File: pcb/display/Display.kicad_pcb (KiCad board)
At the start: 2 copper layers, 100 x 75 mm, 181 parts, among them J1 Screw_Terminal_01x04, J10 XH 2P, J11 XH 2P, J12 XH 2P, J13 XH 2P, J14 XH 2P, J15 XH 2P, J16 XH 2P, J17 XH 2P, J18 XH 2P, J19 XH 2P, J2 RJ45, J20 XH 2P, J4 Conn_01x08_Pin, J5 Term, J6 Term, J7 XH 2P, J8 XH 2P, J9 XH 2P, P1 USB_C_Plug_USB2.0, Q1 60N03D, Q10 60N03D, Q11 60N03D, Q12 60N03D, Q13 60N03D, Q14 60N03D, Q15 60N03D, Q16 60N03D, Q2 60N03D, Q3 60N03D, Q4 60N03D, Q5 60N03D, Q6 60N03D, Q7 60N03D, Q8 60N03D, Q9 60N03D, SW1 SW_Push, SW2 SW_Push, SW3 SW_Push, SW4 SW_Push, U1 TMP1075DSG, U10 TPS259474x, U11 LV3842, U2 ESP32-S3-MINI-1, U3 TPS22810DRV, U4 TCA9535RGER, U5 SP3485EN, U6 AP2210, U7 Ai-Thinker-Ra-02, U8 E220-400M22S, U9 SIC438BED-T1-GE3

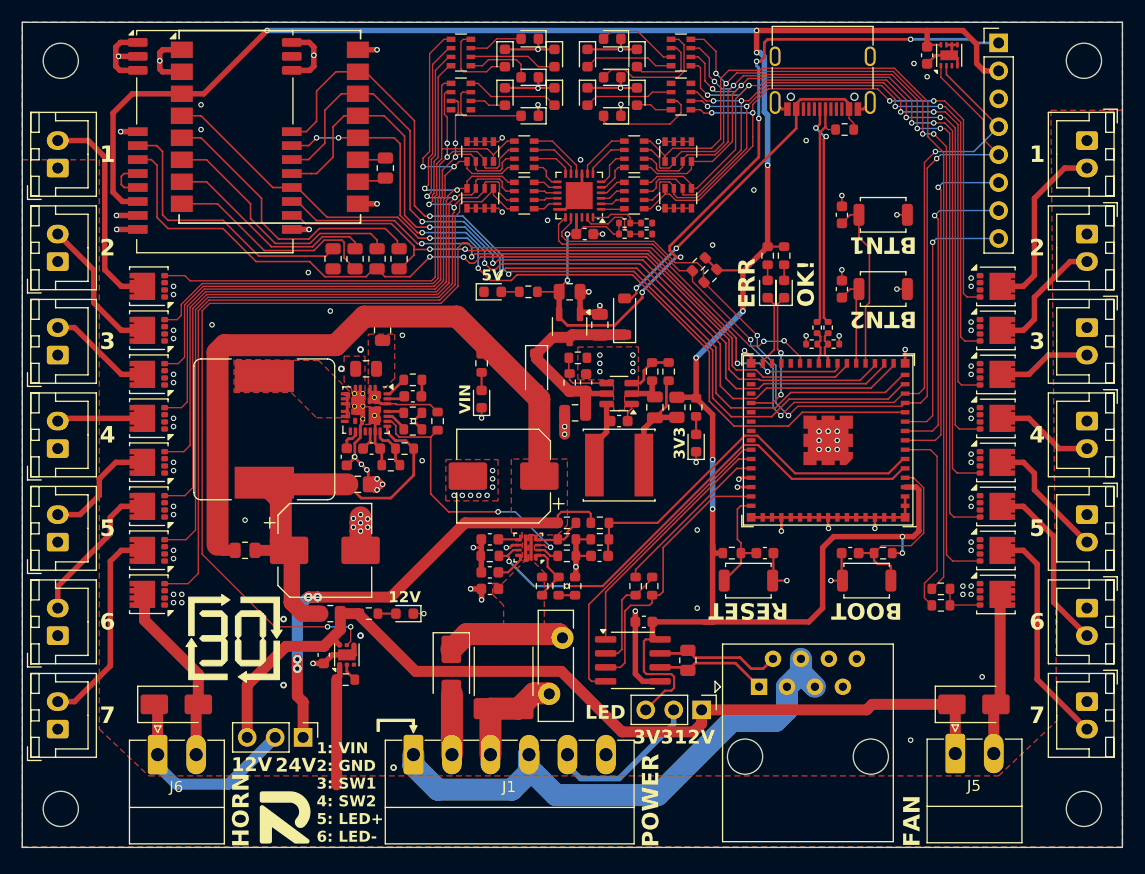
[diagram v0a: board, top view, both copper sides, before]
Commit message: Final Version of Prototype Rev. 00
Switched back to PCA9685 for PWM, removed high side switch
Updated some component values
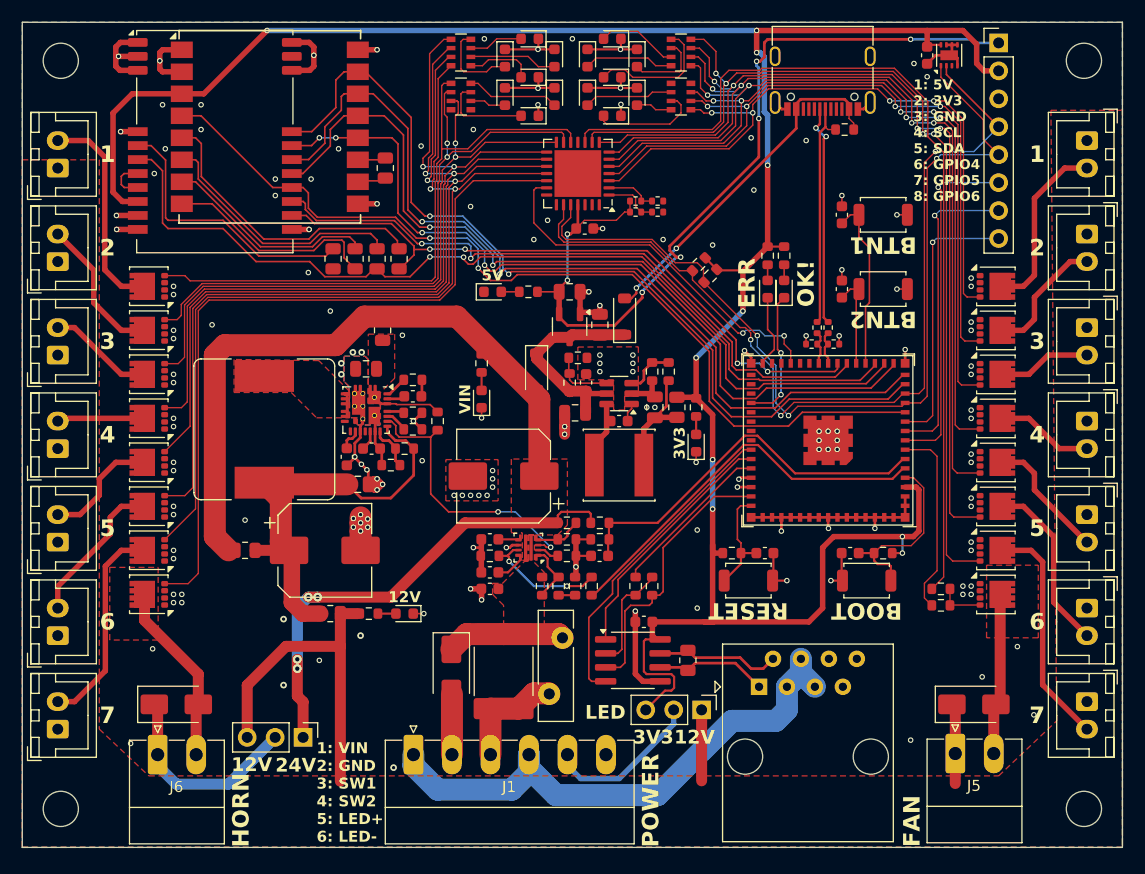
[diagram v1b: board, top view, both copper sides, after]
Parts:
- removed C5: 100nF, Capacitor_SMD:C_0603_1608Metric
- removed the G*** at (77.5, 122.0)
- removed the REF** at (69.0, 106.0)
- removed RN1, RN2, RN3, RN4: 10R, Resistor_SMD:R_Array_Convex_4x0603
- removed RN5, RN6, RN7, RN8: 10k, Resistor_SMD:R_Array_Convex_4x0603
- removed U3: TPS22810DRV, Package_SON:WSON-6-1EP_2x2mm_P0.65mm_EP1x1.6mm
- added G***: LOGO, RVNSPRK_Markings:JLC-UL_1-2Layer_10mm, B.Cu at (100.0, 91.2)
- added G***: LOGO, Open-Shot-Clock:Open-Shot-Clock_QR_8mm, B.Cu at (108.7, 120.8)
- added REF**: OSHW-Logo2_7.3x6mm_SilkScreen, Symbol:OSHW-Logo2_7.3x6mm_SilkScreen, B.Cu at (136.5, 121.5)
- C10, C11: value 100n -> 10p
- C6: value 100nF -> 100n
- D1, D2: value D_Schottky -> SMAJ24A
- D18, D19: value D_Schottky -> B5819W
- G***: footprint RVNSPRK_Logo:Ravnsprk_Logo_5mm -> RVNSPRK_Logo:Ravnsprk_Logo_Mask_5mm; moved to B.Cu
- J1: value Screw_Terminal_01x04 -> Screw Terminal 3.5mm
- J4: value Conn_01x08_Pin -> 01x08_Pin
- J5, J6: value Term -> Term 3.5mm
- L3: value 10u -> 10uH
- Q1, Q10, Q11, Q12, Q13, Q14, Q15, Q16, Q2, Q3, Q4, Q5, Q6, Q7, Q8, Q9: value 60N03D -> 20N06
- R10, R46, R47: value 20k -> 4k3
- R17, R35, R43: value 20k -> 1k
- R18, R34: value 20k -> 10k
- R2: value 10R -> 1k
- R33: value 20k -> 22k
- R48, R49, R50, R51: value 10R -> 0R
- R8, R9: value 1k -> 0R
- RN09, RN10, RN11, RN12: value 10R -> 3k3
- SW1, SW2, SW3, SW4: value SW_Push -> SW_4x3mm
- U4: value TCA9535RGER -> PCA9685BS; footprint Package_DFN_QFN:VQFN-24-1EP_4x4mm_P0.5mm_EP2.45x2.45mm -> Package_DFN_QFN:QFN-28-1EP_6x6mm_P0.65mm_EP4.25x4.25mm
- moved R2 23.9 mm to (101.8, 101.2), turned to -90 degrees
- moved REF** 21.3 mm to (121.2, 121.2)
- moved REF** 6.15 mm to (100.5, 61.6)
- moved G*** 3.34 mm to (77.2, 121.5), turned to 180 degrees
- moved R48 2.24 mm to (107.8, 66.2)
- moved R49 2.24 mm to (107.8, 67.2)
- moved R50 2.24 mm to (105.8, 67.2)
- moved R51 2.24 mm to (105.8, 66.2)
- moved U4 2.00 mm to (100.5, 63.8)
- moved C6 0.50 mm to (101.1, 68.8)
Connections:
- J10 pad 1: +12P -> +12V
- J11 pad 1: +12P -> +12V
- J12 pad 1: +12P -> +12V
- J13 pad 1: +12P -> +12V
- J14 pad 1: +12P -> +12V
- J15 pad 1: +12P -> +12V
- J16 pad 1: +12P -> +12V
- J17 pad 1: +12P -> +12V
- J18 pad 1: +12P -> +12V
- J19 pad 1: +12P -> +12V
- J20 pad 1: +12P -> +12V
- J7 pad 1: +12P -> +12V
- J8 pad 1: +12P -> +12V
- J9 pad 1: +12P -> +12V
- R2 pad 1: +12P -> Net-(U10-ILIM)
- R2 pad 2: Net-(U3-QOD) -> /I_SENSE
- R25 pad 1: /I_SENSE -> Net-(U10-ILIM)
- R45 pad 2: Net-(RN2-R4.1) -> Net-(U4-LED7)
- R48 pad 1: Net-(U4-A2) -> Net-(U4-A4)
- R49 pad 1: Net-(U4-A1) -> Net-(U4-A3)
- R50 pad 2: Net-(U4-A1) -> Net-(U4-A3)
- R51 pad 2: Net-(U4-A2) -> Net-(U4-A4)
- U10 pad 9: /I_SENSE -> Net-(U10-ILIM)
- U2 pad 26: /BRIGHTNESS -> unconnected-(U2-GPIO26-Pad26)
- U2 pad 27: unconnected-(U2-GPIO47/SPICLK_P/SUBSPICLK_P_DIFF-Pad27) -> /PWM.OE
- U4 pad 1: Net-(RN1-R1.2) -> Net-(U4-A3)
- U4 pad 10: Net-(RN3-R1.2) -> Net-(U4-LED7)
- U4 pad 11: Net-(RN3-R2.2) -> GND
- U4 pad 12: Net-(RN3-R3.2) -> /LED Driver/7-Segment1/Segment1
- U4 pad 13: Net-(RN3-R4.2) -> /LED Driver/7-Segment1/Segment2
- U4 pad 14: Net-(RN4-R1.2) -> /LED Driver/7-Segment1/Segment3
- U4 pad 15: Net-(RN4-R2.2) -> /LED Driver/7-Segment1/Segment4
- U4 pad 16: Net-(RN4-R3.2) -> /LED Driver/7-Segment1/Segment5
- U4 pad 17: Net-(RN4-R4.2) -> /LED Driver/7-Segment1/Segment6
- U4 pad 18: GND -> /LED Driver/7-Segment1/Segment7
- U4 pad 19: /I2C.SCL -> Net-(Q2-G)
- U4 pad 2: Net-(RN1-R2.2) -> Net-(U4-A4)
- U4 pad 20: /I2C.SDA -> /PWM.OE
- U4 pad 21: +5V -> GND
- U4 pad 23: Net-(U4-A1) -> /I2C.SCL
- U4 pad 24: Net-(U4-A2) -> /I2C.SDA
- U4 pad 25: GND -> +5V
- U4 pad 3: Net-(RN1-R3.2) -> /LED Driver/7-Segment2/Segment1
- U4 pad 4: Net-(RN1-R4.2) -> /LED Driver/7-Segment2/Segment2
- U4 pad 5: Net-(RN2-R1.2) -> /LED Driver/7-Segment2/Segment3
- U4 pad 6: Net-(RN2-R2.2) -> /LED Driver/7-Segment2/Segment4
- U4 pad 7: Net-(RN2-R3.2) -> /LED Driver/7-Segment2/Segment5
- U4 pad 8: Net-(RN2-R4.2) -> /LED Driver/7-Segment2/Segment6
- U4 pad 9: GND -> /LED Driver/7-Segment2/Segment7
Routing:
- net /BRIGHTNESS: track 104.4 -> 0.00 mm, vias 4 -> 0
- net Net-(U4-LED7): track 0.00 -> 83.3 mm
- net Net-(RN2-R4.1): track 80.1 -> 0.00 mm
- net +12V: track 85.4 -> 45.3 mm
- net /PWM.OE: track 0.00 -> 34.2 mm, vias 0 -> 2
- net GND: track 186.5 -> 163.2 mm, vias 146 -> 164
- net Net-(U10-ILIM): track 0.00 -> 11.3 mm, vias 0 -> 2
- net +12P: track 11.1 -> 0.00 mm
- net /I_SENSE: track 46.5 -> 35.8 mm, vias 2 -> 0
- net Net-(U4-A1): track 6.59 -> 0.00 mm
- net Net-(RN3-R1.2): track 5.52 -> 0.00 mm
- net /LED Driver/7-Segment1/Segment1: track 51.5 -> 56.9 mm
- net Net-(U4-A2): track 5.10 -> 0.00 mm
- net Net-(RN2-R4.2): track 5.02 -> 0.00 mm
- net Net-(U4-A3): track 0.00 -> 5.00 mm
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- added copper zone on F.Cu, net +12V
- added copper zone on F.Cu, net Net-(D1-A2)
- added copper zone on F.Cu, net Net-(D2-A2)
- removed copper zone on F.Cu, net +12P
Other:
- board text added: "1: 5V 2: 3V3 3: GND 4: SCL 5: SDA 6: GPIO4 7: GPIO5 8: GPIO6"
- board text added: "Open Shot Clock Display"
- board text added: "Rev. 00 яαvεηsραяκ 2024"
- board text removed: "Open Shot Clock Display Driver"
- board text removed: "R00 яαvεηsραяκ 2024"

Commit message: Display HW Revision 01
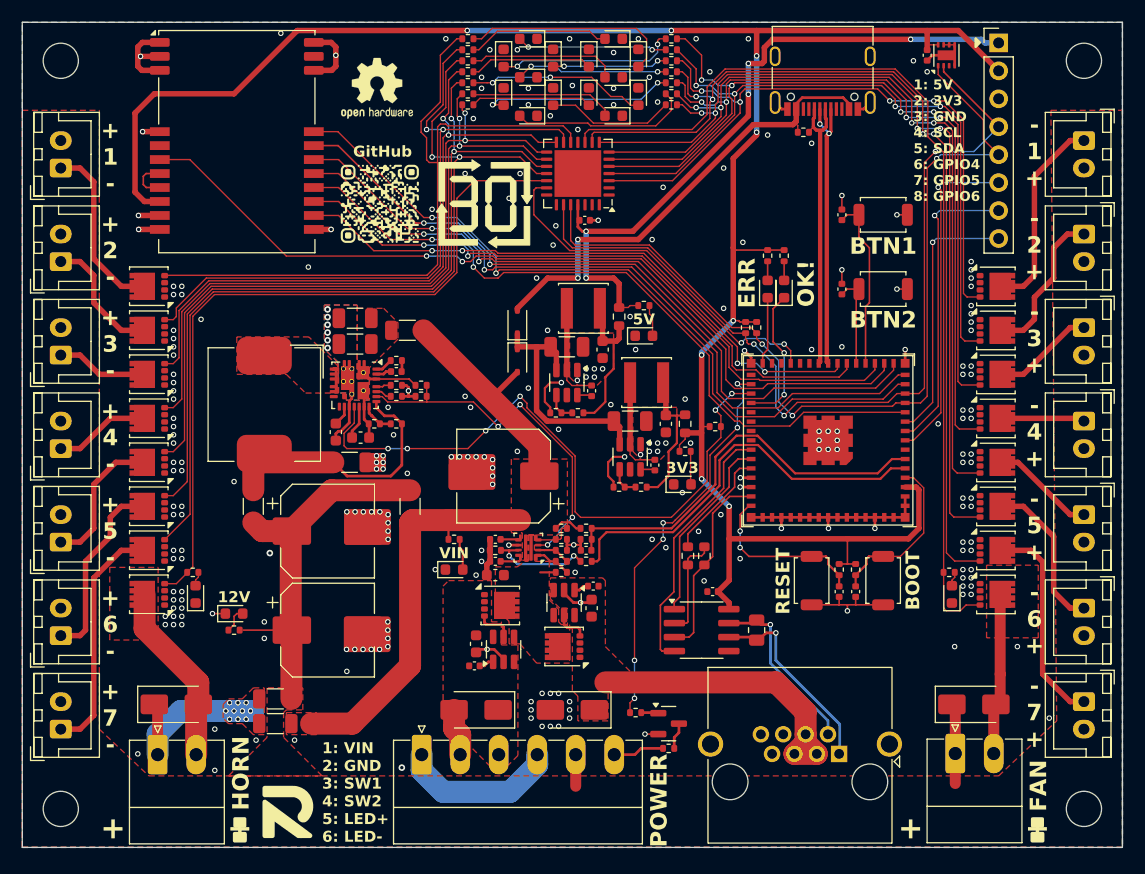
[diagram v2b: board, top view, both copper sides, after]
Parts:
- removed C10, C11: 10p, Resistor_SMD:R_0402_1005Metric
- removed C21, C9: 100n, Capacitor_SMD:C_0603_1608Metric
- removed C22, C24: 1u, Capacitor_SMD:C_0805_2012Metric
- removed C23, C25: 10u, Capacitor_SMD:C_0805_2012Metric
- removed D17: SMAJ24A, Diode_SMD:D_SMA
- removed D22: LED, LED_SMD:LED_0603_1608Metric
- removed F1: 2.6A, Fuse:Fuse_2920_7451Metric
- removed F2: 3A, Fuse:Fuse_Bourns_MF-RG400
- removed JP1, JP2: Jumper_3_Open, Connector_PinHeader_2.54mm:PinHeader_1x03_P2.54mm_Vertical
- removed L4: 12uH, Inductor_SMD:L_Changjiang_FNR6045S
- removed R11, R12, R13, R14, R16, R3: 0R, Resistor_SMD:R_0805_2012Metric
- removed R24, R44, R45: 0R, Resistor_SMD:R_0603_1608Metric
- removed R31, R41: 22k, Resistor_SMD:R_0603_1608Metric
- removed R32, R42: 10k, Resistor_SMD:R_0603_1608Metric
- removed R35: 1k, Resistor_SMD:R_0603_1608Metric
- removed R48, R49, R50, R51, R8, R9: 0R, Resistor_SMD:R_0402_1005Metric
- removed RN09, RN10, RN11, RN12: 3k3, Resistor_SMD:R_Array_Convex_4x0603
- removed U11: LV3842, Package_TO_SOT_SMD:SOT-23-6
- removed U6: AP2210, Package_TO_SOT_SMD:SOT-23-3
- removed U7: Ai-Thinker-Ra-02, RF_Module:Ai-Thinker-Ra-01-LoRa
- added C602: 10u, Capacitor_SMD:C_1206_3216Metric, F.Cu at (80.2, 76.9)
- added C608: 100u, Capacitor_SMD:CP_Elec_8x10, F.Cu at (77.8, 105.2)
- added C614: 100n, Capacitor_SMD:C_0402_1005Metric, F.Cu at (107.5, 90.2)
- added C615: 10u, Capacitor_SMD:C_1206_3216Metric, F.Cu at (105.2, 86.2)
- added C616: 10u, Capacitor_SMD:C_0603_1608Metric, F.Cu at (108.5, 86.5)
- added C617: 100n, Capacitor_SMD:C_0402_1005Metric, F.Cu at (101.8, 83.5)
- added C618: 10u, Capacitor_SMD:C_1206_3216Metric, F.Cu at (99.5, 79.5)
- added C619: 10u, Capacitor_SMD:C_0603_1608Metric, F.Cu at (102.8, 79.8)
- added C620: 100n, Capacitor_SMD:C_0402_1005Metric, F.Cu at (91.1, 108.5)
- added C621: 100n, Capacitor_SMD:C_0402_1005Metric, F.Cu at (101.9, 101.2)
- added C622: 1u, Capacitor_SMD:C_0603_1608Metric, F.Cu at (91.2, 106.5)
- added C623: 1u, Capacitor_SMD:C_0603_1608Metric, F.Cu at (101.8, 103.2)
- added D201: LED, LED_SMD:LED_0603_1608Metric, F.Cu at (65.8, 102.0)
- added D203: LED, LED_SMD:LED_0603_1608Metric, F.Cu at (134.5, 102.0)
- added D603: SMAJ24CA, Diode_SMD:D_SMA, F.Cu at (91.2, 112.5)
- added D604: SMAJ24CA, Diode_SMD:D_SMA, F.Cu at (100.0, 112.5)
- added D608: LED, LED_SMD:LED_0603_1608Metric, F.Cu at (110.0, 92.0)
- added G***: LOGO, RVNSPRK_Logo:Ravnsprk_Logo_5mm, F.Cu at (74.2, 121.8)
- added L602: 33uH, Inductor_SMD:L_Changjiang_FNR4030S, F.Cu at (106.8, 82.8)
- added L603: 33uH, Inductor_SMD:L_Changjiang_FNR4030S, F.Cu at (101.0, 76.0)
- added Q101: 2N7002, Package_TO_SOT_SMD:SOT-23, F.Cu at (108.8, 113.8)
- added Q601: DOZ35N06, Package_SON:VSON-8_3.3x3.3mm_P0.65mm_NexFET, F.Cu at (93.5, 103.0)
- added Q602: DOZ35N06, Package_SON:VSON-8_3.3x3.3mm_P0.65mm_NexFET, F.Cu at (99.2, 106.8)
- added R104: 1k8, Resistor_SMD:R_0402_1005Metric, F.Cu at (105.8, 112.8)
- added R105: 1k8, Resistor_SMD:R_0402_1005Metric, F.Cu at (108.8, 116.0)
- added R110: 18k, Resistor_SMD:R_0402_1005Metric, F.Cu at (113.0, 86.8)
- added R201: 0R, Resistor_SMD:R_1206_3216Metric, F.Cu at (73.0, 113.8)
- added R202: 0R, Resistor_SMD:R_1206_3216Metric, F.Cu at (73.0, 111.5)
- added R203: 4k3, Resistor_SMD:R_0402_1005Metric, F.Cu at (65.5, 100.0)
- added R204: 4k3, Resistor_SMD:R_0402_1005Metric, F.Cu at (134.2, 100.0)
- added R401: 4k3, Resistor_SMD:R_0402_1005Metric, F.Cu at (90.5, 53.5)
- added R402: 4k3, Resistor_SMD:R_0402_1005Metric, F.Cu at (90.5, 55.5)
- added R403: 4k3, Resistor_SMD:R_0402_1005Metric, F.Cu at (90.5, 56.5)
- added R404: 4k3, Resistor_SMD:R_0402_1005Metric, F.Cu at (90.5, 57.5)
- added R405: 4k3, Resistor_SMD:R_0402_1005Metric, F.Cu at (90.5, 54.5)
- added R406: 4k3, Resistor_SMD:R_0402_1005Metric, F.Cu at (90.5, 52.5)
- added R407: 4k3, Resistor_SMD:R_0402_1005Metric, F.Cu at (90.5, 51.5)
- added R501: 4k3, Resistor_SMD:R_0402_1005Metric, F.Cu at (109.0, 54.5)
- added R502: 4k3, Resistor_SMD:R_0402_1005Metric, F.Cu at (109.0, 57.5)
- added R503: 4k3, Resistor_SMD:R_0402_1005Metric, F.Cu at (109.0, 56.5)
- added R504: 4k3, Resistor_SMD:R_0402_1005Metric, F.Cu at (109.0, 55.5)
- added R505: 4k3, Resistor_SMD:R_0402_1005Metric, F.Cu at (109.0, 51.5)
- added R506: 4k3, Resistor_SMD:R_0402_1005Metric, F.Cu at (109.0, 52.5)
- added R507: 4k3, Resistor_SMD:R_0402_1005Metric, F.Cu at (109.0, 53.5)
- added R612: 4k3, Resistor_SMD:R_0402_1005Metric, F.Cu at (86.2, 84.0)
- added R620: 0R, Resistor_SMD:R_0603_1608Metric, F.Cu at (110.2, 86.5)
- added R621: 82k, Resistor_SMD:R_0402_1005Metric, F.Cu at (106.2, 92.2)
- added R622: 18k, Resistor_SMD:R_0402_1005Metric, F.Cu at (104.2, 92.2)
- added R623: 0R, Resistor_SMD:R_0603_1608Metric, F.Cu at (104.2, 76.8)
- added R624: 82k, Resistor_SMD:R_0402_1005Metric, F.Cu at (100.5, 85.5)
- added R625: 11k, Resistor_SMD:R_0402_1005Metric, F.Cu at (98.5, 85.5)
- added R629: 1k8, Resistor_SMD:R_0402_1005Metric, F.Cu at (110.2, 89.0)
- added U603: TPS54202DDC, Package_TO_SOT_SMD:SOT-23-6, F.Cu at (105.2, 89.5)
- added U604: TPS54202DDC, Package_TO_SOT_SMD:SOT-23-6, F.Cu at (99.5, 82.8)
- added U605: LM74700, Package_TO_SOT_SMD:SOT-23-6, F.Cu at (93.8, 107.0)
- added U606: LM74700, Package_TO_SOT_SMD:SOT-23-6, F.Cu at (99.2, 102.8)
- C101: renamed from C3; footprint Capacitor_SMD:C_0603_1608Metric -> Capacitor_SMD:C_0402_1005Metric
- C102: renamed from C4; footprint Capacitor_SMD:C_0603_1608Metric -> Capacitor_SMD:C_0402_1005Metric
- C103: renamed from C2; footprint Capacitor_SMD:C_0603_1608Metric -> Capacitor_SMD:C_0402_1005Metric
- C104: renamed from C1; footprint Capacitor_SMD:C_0603_1608Metric -> Capacitor_SMD:C_0402_1005Metric
- C105: renamed from C27; footprint Capacitor_SMD:C_0603_1608Metric -> Capacitor_SMD:C_0402_1005Metric
- C201: renamed from C6; footprint Capacitor_SMD:C_0603_1608Metric -> Capacitor_SMD:C_0402_1005Metric
- C301: renamed from C7; footprint Capacitor_SMD:C_0603_1608Metric -> Capacitor_SMD:C_0402_1005Metric
- C601: renamed from C12; footprint Capacitor_SMD:C_0603_1608Metric -> Capacitor_SMD:C_0402_1005Metric
- C603: renamed from C16; value 1u -> 10u; footprint Capacitor_SMD:C_0805_2012Metric -> Capacitor_SMD:C_1206_3216Metric
- C606: renamed from C19; value 1u -> 10u; footprint Capacitor_SMD:C_0805_2012Metric -> Capacitor_SMD:C_1206_3216Metric
- C609: renamed from C26; value 100n -> 1u
- C610: renamed from C13; value 1u -> 10n; footprint Capacitor_SMD:C_0603_1608Metric -> Capacitor_SMD:C_0402_1005Metric
- C611: renamed from C14; footprint Capacitor_SMD:C_0603_1608Metric -> Capacitor_SMD:C_0402_1005Metric
- C613: renamed from C8; footprint Capacitor_SMD:C_0603_1608Metric -> Capacitor_SMD:C_0402_1005Metric
- D202: renamed from D2; value SMAJ24A -> SS54
- D204: renamed from D1; value SMAJ24A -> SS54
- D601: renamed from D19; value B5819W -> 1N5819WS; footprint Diode_SMD:D_SOD-123 -> Diode_SMD:D_SOD-323
- D602: renamed from D18; value B5819W -> 1N5819WS; footprint Diode_SMD:D_SOD-123 -> Diode_SMD:D_SOD-323
- G***, REF** (x2): moved to F.Cu
- J101: renamed from J2; footprint Connector_RJ:RJ45_Amphenol_54602-x08_Horizontal -> Connector_RJ:RJ45_Amphenol_RJHSE5380
- L601: renamed from L3; value 10uH -> 6.8uH; footprint Inductor_SMD:L_Bourns_SRR1260 -> Inductor_SMD:L_Bourns_SRP1050WA
- Q201: renamed from Q2; value 20N06 -> DOZ35N06
- Q202: renamed from Q1; value 20N06 -> DOZ35N06
- Q401: renamed from Q3; value 20N06 -> DOZ35N06
- Q402: renamed from Q4; value 20N06 -> DOZ35N06
- Q403: renamed from Q5; value 20N06 -> DOZ35N06
- Q404: renamed from Q6; value 20N06 -> DOZ35N06
- Q405: renamed from Q7; value 20N06 -> DOZ35N06
- Q406: renamed from Q8; value 20N06 -> DOZ35N06
- Q407: renamed from Q9; value 20N06 -> DOZ35N06
- Q501: renamed from Q10; value 20N06 -> DOZ35N06
- Q502: renamed from Q11; value 20N06 -> DOZ35N06
- Q503: renamed from Q12; value 20N06 -> DOZ35N06
- Q504: renamed from Q13; value 20N06 -> DOZ35N06
- Q505: renamed from Q14; value 20N06 -> DOZ35N06
- Q506: renamed from Q15; value 20N06 -> DOZ35N06
- Q507: renamed from Q16; value 20N06 -> DOZ35N06
- R101: renamed from R17; value 1k -> 1k8; footprint Resistor_SMD:R_0603_1608Metric -> Resistor_SMD:R_0402_1005Metric
- R102: renamed from R43; value 1k -> 1k8; footprint Resistor_SMD:R_0603_1608Metric -> Resistor_SMD:R_0402_1005Metric
- R103: renamed from R7; footprint Resistor_SMD:R_0603_1608Metric -> Resistor_SMD:R_0402_1005Metric
- R106: renamed from R1; value 1k -> 1k8; footprint Resistor_SMD:R_0603_1608Metric -> Resistor_SMD:R_0402_1005Metric
- R107: renamed from R46; footprint Resistor_SMD:R_0603_1608Metric -> Resistor_SMD:R_0402_1005Metric
- R108: renamed from R47; footprint Resistor_SMD:R_0603_1608Metric -> Resistor_SMD:R_0402_1005Metric
- R109: renamed from R15; value 1k -> 1k8; footprint Resistor_SMD:R_0603_1608Metric -> Resistor_SMD:R_0402_1005Metric
- R601: renamed from R37; footprint Resistor_SMD:R_0805_2012Metric -> Resistor_SMD:R_1206_3216Metric
- R602: renamed from R36; footprint Resistor_SMD:R_0805_2012Metric -> Resistor_SMD:R_1206_3216Metric
- R603: renamed from R18; value 10k -> 18k; footprint Resistor_SMD:R_0603_1608Metric -> Resistor_SMD:R_0402_1005Metric
- R604: renamed from R19; value 10k -> 18k; footprint Resistor_SMD:R_0603_1608Metric -> Resistor_SMD:R_0402_1005Metric
- R605: renamed from R38; footprint Resistor_SMD:R_0603_1608Metric -> Resistor_SMD:R_0402_1005Metric
- R606: renamed from R20; value 10k -> 18k; footprint Resistor_SMD:R_0603_1608Metric -> Resistor_SMD:R_0402_1005Metric
- R607: renamed from R21; value 10k -> 18k; footprint Resistor_SMD:R_0603_1608Metric -> Resistor_SMD:R_0402_1005Metric
- R608: renamed from R40; footprint Resistor_SMD:R_0805_2012Metric -> Resistor_SMD:R_1206_3216Metric
- R609: renamed from R22; value 1k -> 1k8; footprint Resistor_SMD:R_0603_1608Metric -> Resistor_SMD:R_0402_1005Metric
- R610: renamed from R2; value 1k -> 1k8; footprint Resistor_SMD:R_0603_1608Metric -> Resistor_SMD:R_0402_1005Metric
- R611: renamed from R23; footprint Resistor_SMD:R_0603_1608Metric -> Resistor_SMD:R_0402_1005Metric
- R613: renamed from R28; footprint Resistor_SMD:R_0603_1608Metric -> Resistor_SMD:R_0402_1005Metric
- R614: renamed from R29; footprint Resistor_SMD:R_0603_1608Metric -> Resistor_SMD:R_0402_1005Metric
- R615: renamed from R30; footprint Resistor_SMD:R_0603_1608Metric -> Resistor_SMD:R_0402_1005Metric
- R616: renamed from R39; value 560R -> 0R; footprint Resistor_SMD:R_0603_1608Metric -> Resistor_SMD:R_0402_1005Metric
- R617: renamed from R25; value 560R -> 680R; footprint Resistor_SMD:R_0603_1608Metric -> Resistor_SMD:R_0402_1005Metric
- R618: renamed from R26; value 1k -> 1k8; footprint Resistor_SMD:R_0603_1608Metric -> Resistor_SMD:R_0402_1005Metric
- R619: renamed from R27; value 1k -> 1k8; footprint Resistor_SMD:R_0603_1608Metric -> Resistor_SMD:R_0402_1005Metric
- R626: renamed from R33; value 22k -> 18k; footprint Resistor_SMD:R_0603_1608Metric -> Resistor_SMD:R_0402_1005Metric
- R627: renamed from R34; value 10k -> 11k; footprint Resistor_SMD:R_0603_1608Metric -> Resistor_SMD:R_0402_1005Metric
- R628: renamed from R10; footprint Resistor_SMD:R_0603_1608Metric -> Resistor_SMD:R_0402_1005Metric
- U101: renamed from U1; value TMP1075DSG -> TMP1075DSGR
- U102: renamed from U2; value ESP32-S3-MINI-1 -> ESP32-S3-MINI-1U-N8
- U301: renamed from U5; value SP3485EN -> SP3485EN-L/TR
- U602: renamed from U10; value TPS259474x -> TPS259474ARPWR
- moved REF** 85.0 mm to (82.2, 56.0), turned to 0 degrees
- moved G*** 60.3 mm to (82.5, 66.5), turned to 0 degrees
- moved REF** 24.8 mm to (96.5, 121.2)
- moved R626 16.2 mm to (89.2, 97.0), turned to 0 degrees
- moved D605 15.7 mm to (89.2, 99.8), turned to 0 degrees
- moved R601 15.5 mm to (85.2, 94.0), turned to 90 degrees
- moved D606 15.5 mm to (69.2, 103.8), turned to 0 degrees
- moved D607 14.3 mm to (106.5, 78.5)
- moved R627 12.3 mm to (69.2, 105.2), turned to 180 degrees
- moved D402 12.1 mm to (106.0, 56.8)
- moved D407 12.1 mm to (106.0, 53.2)
- moved D504 12.1 mm to (93.8, 56.8)
- moved D505 12.1 mm to (93.8, 53.2)
- moved R608 12.0 mm to (71.0, 94.0), turned to 90 degrees
- moved R628 10.6 mm to (106.5, 75.8), turned to 0 degrees
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- renumbered C17 to C604, C18 to C605, C20 to C607, C15 to C612, D24 to D101, D25 to D102, D16 to D401, D12 to D402, D11 to D403, D10 to D404, D15 to D405, D14 to D406, D13 to D407, D9 to D501, D5 to D502, D4 to D503, D3 to D504, D8 to D505, D7 to D506, D6 to D507, D20 to D605, D21 to D606, D23 to D607, H1 to H101, H2 to H102, H3 to H103, H4 to H104, J1 to J102, J4 to J103, J6 to J201, J5 to J202, J7 to J401, J8 to J402, J9 to J403, J10 to J404, J11 to J405, J12 to J406, J13 to J407, J14 to J501, J15 to J502, J16 to J503, J17 to J504, J18 to J505, J19 to J506, J20 to J507, P1 to P101, R4 to R301, R5 to R302, R6 to R303, SW2 to SW101, SW3 to SW102, SW1 to SW103, SW4 to SW104, U4 to U201, U8 to U302, U9 to U601
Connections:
- net /LED Driver/7-Segment1/Segment1 renamed /LED Driver/7-Segment1 units/Segment1
- net /LED Driver/7-Segment1/Segment2 renamed /LED Driver/7-Segment1 units/Segment2
- net /LED Driver/7-Segment1/Segment3 renamed /LED Driver/7-Segment1 units/Segment3
- net /LED Driver/7-Segment1/Segment4 renamed /LED Driver/7-Segment1 units/Segment4
- net /LED Driver/7-Segment1/Segment5 renamed /LED Driver/7-Segment1 units/Segment5
- net /LED Driver/7-Segment1/Segment6 renamed /LED Driver/7-Segment1 units/Segment6
- net /LED Driver/7-Segment1/Segment7 renamed /LED Driver/7-Segment1 units/Segment7
- net /LED Driver/7-Segment2/Segment1 renamed /LED Driver/7-Segment2 tens/Segment1
- net /LED Driver/7-Segment2/Segment2 renamed /LED Driver/7-Segment2 tens/Segment2
- net /LED Driver/7-Segment2/Segment3 renamed /LED Driver/7-Segment2 tens/Segment3
- net /LED Driver/7-Segment2/Segment4 renamed /LED Driver/7-Segment2 tens/Segment4
- net /LED Driver/7-Segment2/Segment5 renamed /LED Driver/7-Segment2 tens/Segment5
- net /LED Driver/7-Segment2/Segment6 renamed /LED Driver/7-Segment2 tens/Segment6
- net /LED Driver/7-Segment2/Segment7 renamed /LED Driver/7-Segment2 tens/Segment7
- net Net-(D17-A1) renamed V1
- C606 pad 1: Net-(U9-VOUT) -> Net-(U601-VOUT)
- C607 pad 1: Net-(U9-VOUT) -> +12V
- J101 pad 3: Net-(J1-Pin_1) -> VBUS
- J101 pad 4: Net-(J1-Pin_1) -> VBUS
- J101 pad 5: Net-(J1-Pin_1) -> VBUS
- J102 pad 1: Net-(J1-Pin_1) -> Net-(J102-Pin_1)
- J102 pad 3: VBUS -> VEXT
- J102 pad 4: Net-(J1-Pin_1) -> Net-(J102-Pin_1)
- J102 pad 5: Net-(J1-Pin_5) -> +12V
- J102 pad 6: GND -> Net-(J102-Pin_6)
- J401 pad 1: +12V -> Net-(J401-Pin_1)
- J401 pad 2: Net-(J7-Pin_2) -> +12V
- J402 pad 1: +12V -> Net-(J402-Pin_1)
- J402 pad 2: Net-(J8-Pin_2) -> +12V
- J403 pad 1: +12V -> Net-(J403-Pin_1)
- J403 pad 2: Net-(J9-Pin_2) -> +12V
- J404 pad 1: +12V -> Net-(J404-Pin_1)
- J404 pad 2: Net-(J10-Pin_2) -> +12V
- J405 pad 1: +12V -> Net-(J405-Pin_1)
- J405 pad 2: Net-(J11-Pin_2) -> +12V
- J406 pad 1: +12V -> Net-(J406-Pin_1)
- J406 pad 2: Net-(J12-Pin_2) -> +12V
- J407 pad 1: +12V -> Net-(J407-Pin_1)
- J407 pad 2: Net-(J13-Pin_2) -> +12V
- J501 pad 1: +12V -> Net-(J501-Pin_1)
- J501 pad 2: Net-(J14-Pin_2) -> +12V
- J502 pad 1: +12V -> Net-(J502-Pin_1)
- J502 pad 2: Net-(J15-Pin_2) -> +12V
- J503 pad 1: +12V -> Net-(J503-Pin_1)
- J503 pad 2: Net-(J16-Pin_2) -> +12V
- J504 pad 1: +12V -> Net-(J504-Pin_1)
- J504 pad 2: Net-(J17-Pin_2) -> +12V
- J505 pad 1: +12V -> Net-(J505-Pin_1)
- J505 pad 2: Net-(J18-Pin_2) -> +12V
- J506 pad 1: +12V -> Net-(J506-Pin_1)
- J506 pad 2: Net-(J19-Pin_2) -> +12V
- J507 pad 1: +12V -> Net-(J507-Pin_1)
- J507 pad 2: Net-(J20-Pin_2) -> +12V
- L601 pad 2: Net-(U9-VOUT) -> Net-(U601-VOUT)
- P101 pad A8: (no net) -> unconnected-(P101-SBU1-PadA8)
- P101 pad B6: (no net) -> /D_P
- P101 pad B7: (no net) -> /D_N
- P101 pad B8: (no net) -> unconnected-(P101-SBU2-PadB8)
- Q202 pad 4: Net-(Q1-G) -> Net-(Q202-G)
- Q401 pad 5: Net-(J7-Pin_2) -> Net-(J401-Pin_1)
- Q402 pad 5: Net-(J8-Pin_2) -> Net-(J402-Pin_1)
- Q403 pad 5: Net-(J9-Pin_2) -> Net-(J403-Pin_1)
- Q404 pad 5: Net-(J10-Pin_2) -> Net-(J404-Pin_1)
- Q405 pad 5: Net-(J11-Pin_2) -> Net-(J405-Pin_1)
- Q406 pad 5: Net-(J12-Pin_2) -> Net-(J406-Pin_1)
- Q407 pad 5: Net-(J13-Pin_2) -> Net-(J407-Pin_1)
- Q501 pad 5: Net-(J14-Pin_2) -> Net-(J501-Pin_1)
- Q502 pad 5: Net-(J15-Pin_2) -> Net-(J502-Pin_1)
- Q503 pad 5: Net-(J16-Pin_2) -> Net-(J503-Pin_1)
- Q504 pad 5: Net-(J17-Pin_2) -> Net-(J504-Pin_1)
- Q505 pad 5: Net-(J18-Pin_2) -> Net-(J505-Pin_1)
- Q506 pad 5: Net-(J19-Pin_2) -> Net-(J506-Pin_1)
- Q507 pad 5: Net-(J20-Pin_2) -> Net-(J507-Pin_1)
- R601 pad 2: Net-(U9-VOUT) -> +12V
- R608 pad 1: Net-(U9-VOUT) -> +12V
- R608 pad 2: +12V -> Net-(U601-VOUT)
- R609 pad 2: Net-(R22-Pad2) -> Net-(U602-OVLO)
- R611 pad 2: Net-(U9-VOUT) -> Net-(U601-VOUT)
- R616 pad 1: Net-(R22-Pad2) -> Net-(U602-OVLO)
- U102 pad 23: /USB.D- -> /D_N
- U102 pad 24: /USB.D+ -> /D_P
- U102 pad 32: unconnected-(U2-SPIIO7/GPIO36/FSPICLK/SUBSPICLK-Pad32) -> /LED.STATUS
- U102 pad 33: unconnected-(U2-SPIDQS/GPIO37/FSPIQ/SUBSPIQ-Pad33) -> /12V_PG
- U201 pad 1: Net-(U4-A3) -> GND
- U201 pad 10: Net-(U4-LED7) -> Net-(Q202-G)
- U201 pad 2: Net-(U4-A4) -> GND
- U302 pad 5: Net-(U8-DIO3) -> unconnected-(U302-DIO3-Pad5)
- U601 pad 14: unconnected-(U9-PGOOD-Pad14) -> /12V_PG
- U601 pad 18: Net-(U9-VOUT) -> Net-(U601-VOUT)
- U602 pad 2: Net-(U10-OVLO) -> Net-(U602-OVLO)
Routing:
- net Net-(Q202-G): track 0.00 -> 87.4 mm
- net Net-(U4-LED7): track 83.3 -> 0.00 mm
- net /12V_PG: track 0.00 -> 59.2 mm, vias 0 -> 6
- net GND: track 163.2 -> 107.7 mm, vias 164 -> 258
- net Net-(J1-Pin_1): track 50.5 -> 0.00 mm
- net VCC: track 104.6 -> 59.9 mm, vias 4 -> 0
- net Net-(U9-VOUT): track 40.2 -> 0.00 mm
- net /LED.STATUS: track 0.00 -> 36.1 mm, vias 0 -> 6
- net +3.3V: track 217.8 -> 189.6 mm, vias 10 -> 8
- net Net-(U7-DIO0): track 26.8 -> 0.00 mm
- net Net-(U601-VOUT): track 0.00 -> 25.8 mm
- net Net-(U8-DIO3): track 25.3 -> 0.00 mm
- net Net-(U7-DIO1): track 23.2 -> 0.00 mm
- net Net-(J407-Pin_1): track 0.00 -> 21.9 mm
- net Net-(J20-Pin_2): track 21.2 -> 0.00 mm
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- added copper zone on F.Cu, net Net-(D202-K)
- added copper zone on F.Cu, net VBUS
- added copper zone on F.Cu, net VEXT
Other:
- board text added: "+"
- board text added: "+ 1 -"
- board text added: "+ 2 -"
- board text added: "+ 3 -"
- board text added: "+ 4 -"
- board text added: "+ 5 -"
- board text added: "+ 6 -"
- board text added: "+ 7 -"
- board text added: "- 1 +"
- board text added: "- 2 +"
- board text added: "- 3 +"
- board text added: "- 4 +"
- board text added: "- 5 +"
- board text added: "- 6 +"
- board text added: "- 7 +"
- board text added: "GitHub"
- board text added: "Rev. 01 яαvεηsραяκ 2025"
- board text removed: "1"
- board text removed: "2"
- board text removed: "24V"
- board text removed: "3"
- board text removed: "4"
- board text removed: "5"
- board text removed: "6"
- board text removed: "7"
- board text removed: "LED"
- board text removed: "Rev. 00 яαvεηsραяκ 2024"

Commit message: Update some wrong values after import in JLC for production
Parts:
- C607, C608, C612: value 100u -> 150u
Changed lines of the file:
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@@
 	(paper "A4")
 	(title_block
-		(title "Open Shot Clock - Display")
-		(date "2025-04-08")
+		(title "Open Shot Clock Display")
+		(date "2025-04-11")
 		(rev "01")
 		(company "Ravenspark")
@@
 			)
 		)
-		(property "Value" "100u"
+		(property "Value" "150u"
 			(at 0 5.2 0)
 			(layer "F.Fab")
@@
 			)
 		)
-		(property "Value" "100u"
+		(property "Value" "150u"
 			(at 0 5.2 0)
 			(layer "F.Fab")
@@
 		(tags "resistor")
 		(property "Reference" "R204"
-			(at 0 -1.17 360)
+			(at 0 -1.17 0)
 			(layer "F.SilkS")
 			(hide yes)
@@
 		)
 		(property "Value" "4k3"
-			(at 0 1.17 360)
+			(at 0 1.17 0)
 			(layer "F.Fab")
 			(effects
@@
 		)
 		(fp_text user "${REFERENCE}"
-			(at 0 0 360)
+			(at 0 0 0)
 			(layer "F.Fab")
 			(effects
@@
 		(tags "capacitor")
 		(property "Reference" "C620"
-			(at 0 -1.16 360)
+			(at 0 -1.16 0)
 			(layer "F.SilkS")
 			(hide yes)
@@
 		)
 		(property "Value" "100n"
-			(at 0 1.16 360)
+			(at 0 1.16 0)
 			(layer "F.Fab")
 			(effects
@@
 		)
 		(fp_text user "${REFERENCE}"
-			(at 0 0 360)
+			(at 0 0 0)
 			(layer "F.Fab")
 			(effects
@@
 			)
 		)
-		(property "JLC PN" "C5291825"
+		(property "JLC PN" "C15269"
 			(at 0 0 0)
 			(unlocked yes)
@@
 			)
 		)
+		(property "JLC PN" "C15195"
+			(at 0 0 0)
+			(unlocked yes)
+			(layer "F.Fab")
+			(hide yes)
+			(effects
+				(font
+					(size 1 1)
+					(thickness 0.15)
+				)
+			)
+		)
 		(property ki_fp_filters "C_*")
 		(sheetname "Power Supply")
@@
 		(tags "capacitor")
 		(property "Reference" "C621"
-			(at 0 -1.16 360)
+			(at 0 -1.16 0)
 			(layer "F.SilkS")
 			(hide yes)
@@
 		)
 		(property "Value" "100n"
-			(at 0 1.16 360)
+			(at 0 1.16 0)
 			(layer "F.Fab")
 			(effects
@@
 		)
 		(fp_text user "${REFERENCE}"
-			(at 0 0 360)
+			(at 0 0 0)
 			(layer "F.Fab")
 			(effects
@@
 			)
 		)
-		(property "JLC PN" "C5291825"
+		(property "JLC PN" "C15269"
 			(at 0 0 0)
 			(unlocked yes)
@@
 			)
 		)
-		(property "Value" "100u"
+		(property "Value" "150u"
 			(at 0 5.2 0)
 			(layer "F.Fab")
@@
 			)
 		)
+		(property "JLC PN" "C1523"
+			(at 0 0 0)
+			(unlocked yes)
+			(layer "F.Fab")
+			(hide yes)
+			(effects
+				(font
+					(size 1 1)
+					(thickness 0.15)
+				)
+			)
+		)
 		(property ki_fp_filters "C_*")
 		(sheetname "Power Supply")
@@
 		(tags "resistor")
 		(property "Reference" "R203"
-			(at 0 -1.17 360)
+			(at 0 -1.17 0)
 			(layer "F.SilkS")
 			(hide yes)
@@
 		)
 		(property "Value" "4k3"
-			(at 0 1.17 360)
+			(at 0 1.17 0)
 			(layer "F.Fab")
 			(effects
@@
 		)
 		(fp_text user "${REFERENCE}"
-			(at 0 0 360)
+			(at 0 0 0)
 			(layer "F.Fab")
 			(effects
